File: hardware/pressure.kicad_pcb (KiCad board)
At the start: 2 copper layers, 17.5 x 25 mm, 19 parts, among them P1 CON-SENSOR, Q1 2N7002P, U1 M24C64, U2 DRILL, U3 DRILL, U4 DRILL, U5 DRILL

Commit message: pressure bricklet hardware prototype
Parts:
- removed FB1: FILTER, kicad-libraries:0603E
- removed LED1: WS2812B_LED, kicad-libraries:WS2812B_LED
- removed Q1: 2N7002P, kicad-libraries:SOT23GDS
- added C5: 10nF, kicad-libraries:0603E, F.Cu at (179.5, 135.8)
- added C6: 1µF, kicad-libraries:0603E, F.Cu at (179.5, 137.2)
- added C7: 470pF, kicad-libraries:0603E, F.Cu at (193.1, 137.1)
- added L1: 1µH, kicad-libraries:0805E, F.Cu at (189.1, 137.3)
- added L2: INDUCT, kicad-libraries:0603E, F.Cu at (181.2, 138.6)
- added R4: TBD, kicad-libraries:0603E, F.Cu at (192.2, 139.4)
- added R5: TBD, kicad-libraries:0603E, F.Cu at (188.3, 142.8)
- added R6: TBD, kicad-libraries:0603E, F.Cu at (194.1, 142.4)
- added U6: FAN4860, kicad-libraries:UMLP_22, F.Cu at (186.4, 137.8)
- added U7: TLV271, kicad-libraries:SOT23-5, F.Cu at (191.0, 142.9)
- added U8: MPX4115A-SOP, kicad-libraries:SOP8, F.Cu at (182.1, 120.5)
- added U9: MPX_UNI, kicad-libraries:MPX_UNI, F.Cu at (182.1, 131.8)
- C2: value 100nF -> 1µF
- C3: value 100nF -> 4.7µF; footprint kicad-libraries:0603E -> kicad-libraries:0805E
- R1: value 1k -> 10k
- R2: value 0 -> TBD
- R3: value 330 -> TBD
- moved C1 67.1 mm to (191.0, 145.5), turned to 0 degrees
- moved P1 64.9 mm to (182.1, 149.5), turned to 0 degrees
- moved R2 60.8 mm to (189.2, 140.3), turned to 0 degrees
- moved U3 59.9 mm to (197.1, 147.0)
- moved R3 57.2 mm to (186.1, 141.9)
- moved U5 56.9 mm to (197.1, 112.0)
- moved C2 54.9 mm to (186.4, 136.1), turned to 0 degrees
- moved G*** 54.2 mm to (176.3, 138.6)
- moved VAL 53.2 mm to (189.8, 126.8)
- moved R1 52.5 mm to (182.8, 141.9), turned to 0 degrees
- moved C3 51.5 mm to (183.8, 137.2), turned to 270 degrees
- moved G*** 44.9 mm to (174.4, 126.8)
- moved U4 43.6 mm to (167.1, 147.0)
- moved U1 41.1 mm to (172.3, 140.0), turned to 0 degrees
- moved U2 39.5 mm to (167.1, 112.0)
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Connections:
- C1 pad 1: Net-(C1-Pad1) -> 3V3
- C1 pad 2: Net-(C1-Pad2) -> GND
- C2 pad 2: VCC -> 3V3
- C3 pad 1: VCC -> GND
- C3 pad 2: GND -> +5V
- P1 pad 1: Net-(C1-Pad2) -> (no net)
- P1 pad 2: Net-(C1-Pad1) -> GND
- P1 pad 8: (no net) -> Net-(P1-Pad8)
- R1 pad 1: Net-(Q1-PadD) -> GND
- R1 pad 2: VCC -> Net-(P1-Pad8)
- R2 pad 1: GND -> Net-(R2-Pad1)
- R2 pad 2: Net-(C1-Pad1) -> Net-(P1-Pad7)
- R3 pad 1: Net-(LED1-Pad4) -> Net-(R2-Pad1)
- R3 pad 2: Net-(Q1-PadD) -> +5V
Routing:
- net Net-(C7-Pad2): track 0.00 -> 31.8 mm
- net 3V3: track 26.9 -> 56.0 mm, vias 2 -> 4
- net Net-(P1-Pad7): track 1.85 -> 20.6 mm
- net VCC: track 14.8 -> 0.00 mm
- net GND: track 13.6 -> 27.5 mm, vias 12 -> 24
- net Net-(C5-Pad2): track 0.00 -> 9.92 mm
- net Net-(P1-Pad8): track 0.00 -> 9.24 mm, vias 0 -> 2
- net +5V: track 0.00 -> 7.56 mm
- net SCL: track 18.6 -> 12.0 mm
- net Net-(Q1-PadD): track 5.53 -> 0.00 mm
- net Net-(R2-Pad1): track 0.00 -> 4.61 mm
- net Net-(R4-Pad2): track 0.00 -> 3.84 mm
- net Net-(C1-Pad2): track 3.51 -> 0.00 mm
- net Net-(C1-Pad1): track 3.29 -> 0.00 mm
- net Net-(LED1-Pad4): track 2.04 -> 0.00 mm
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- added copper zone on F.Cu, net +5V
- added copper zone on F.Cu, net 3V3
- added copper zone on F.Cu, net GND
- added copper zone on F.Cu, net Net-(R4-Pad2)
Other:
- board size 17.5 x 25 mm -> 35 x 40 mm
- board text added: "Pressure 1.0"
- board text removed: "RGB LED 1.0"

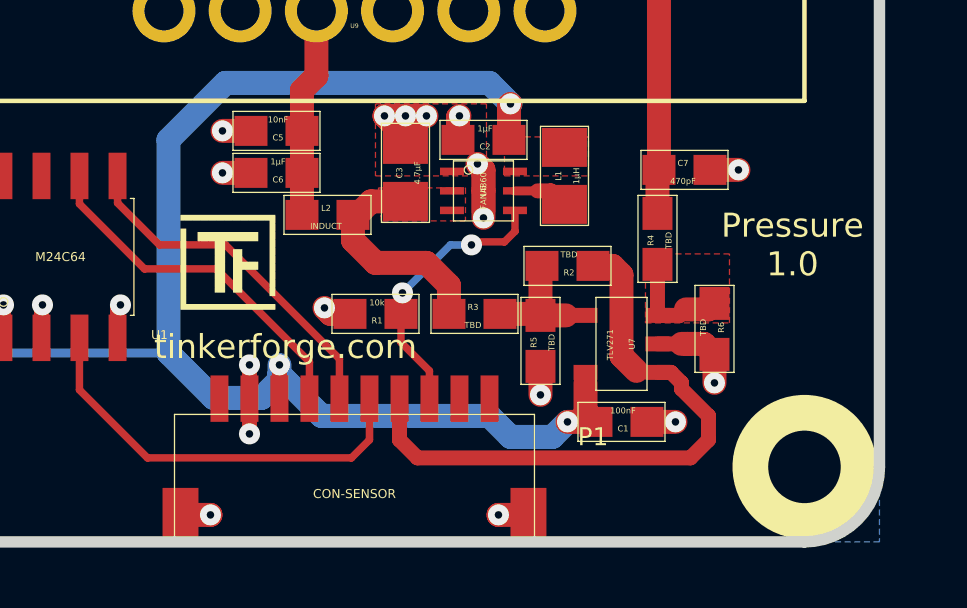
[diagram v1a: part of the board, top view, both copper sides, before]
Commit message: todo: fix input direction
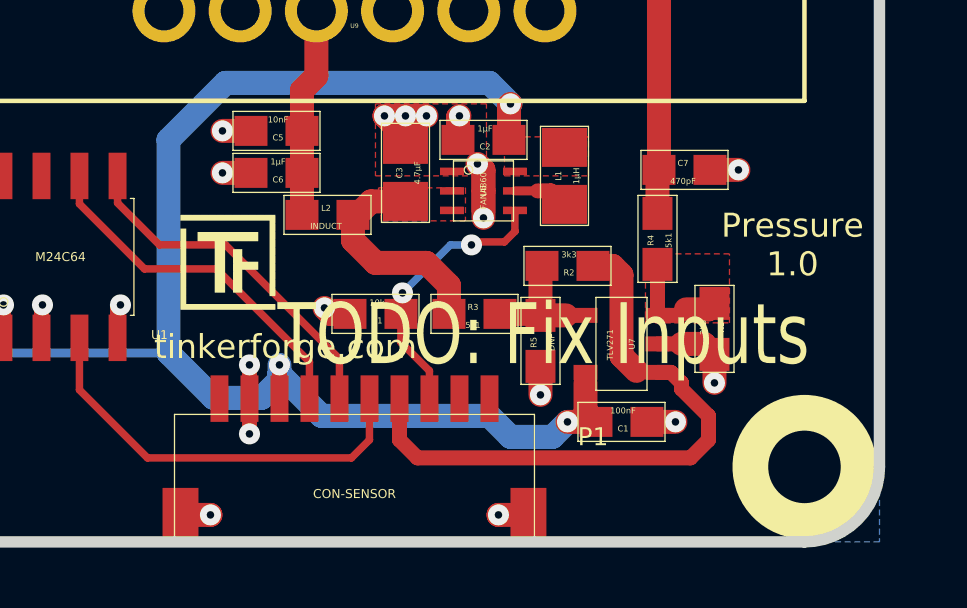
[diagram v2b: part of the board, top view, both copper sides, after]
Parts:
- R2, R6: value TBD -> 3k3
- R3, R4: value TBD -> 5k1
- R5: value TBD -> DNP
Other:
- board text added: "TODO: Fix Inputs"
